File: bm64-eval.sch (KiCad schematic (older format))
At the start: 52 parts, among them J1 BATTERY, J2 USB, J3 HEADPHONE, J4 MIC, J5 EXT_1, J6 EXT_2, J7 EXT_3, J8 EXT_5, J9 EXT_4, SW1 RESET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

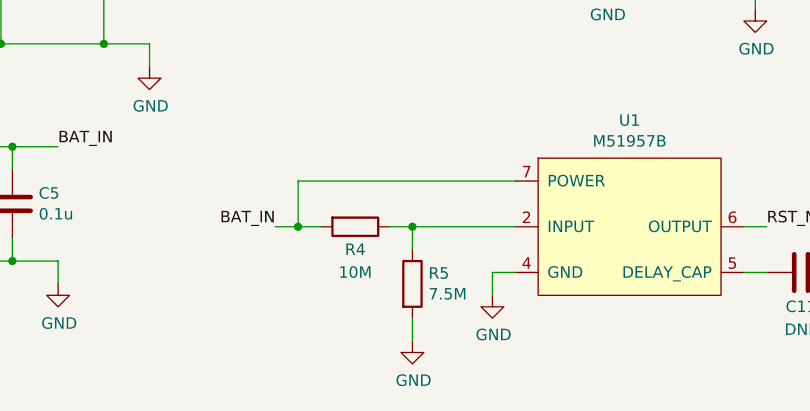
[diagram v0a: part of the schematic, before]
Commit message: swap R4 R5 value
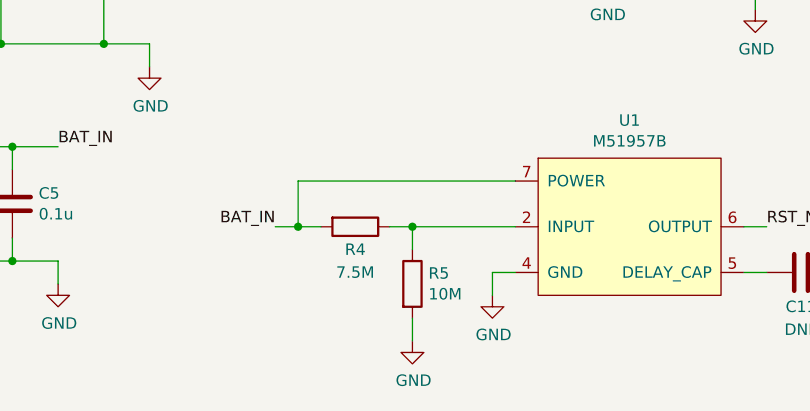
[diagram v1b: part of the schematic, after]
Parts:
- R4: value 10M -> 7.5M
- R5: value 7.5M -> 10M
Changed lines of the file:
@@
 P 3600 6950
 F 0 "R4" V 3700 6950 50  0000 C CNN
-F 1 "10M" V 3800 6950 50  0000 C CNN
+F 1 "7.5M" V 3800 6950 50  0000 C CNN
 F 2 "Resistor_SMD:R_0603_1608Metric" V 3530 6950 50  0001 C CNN
 F 3 "~" H 3600 6950 50  0001 C CNN
@@
 P 3850 7200
 F 0 "R5" H 3920 7246 50  0000 L CNN
-F 1 "7.5M" H 3920 7155 50  0000 L CNN
+F 1 "10M" H 3920 7155 50  0000 L CNN
 F 2 "Resistor_SMD:R_0603_1608Metric" V 3780 7200 50  0001 C CNN
 F 3 "~" H 3850 7200 50  0001 C CNN
